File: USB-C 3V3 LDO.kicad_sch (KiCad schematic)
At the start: 6 parts, among them U7 TPS76333

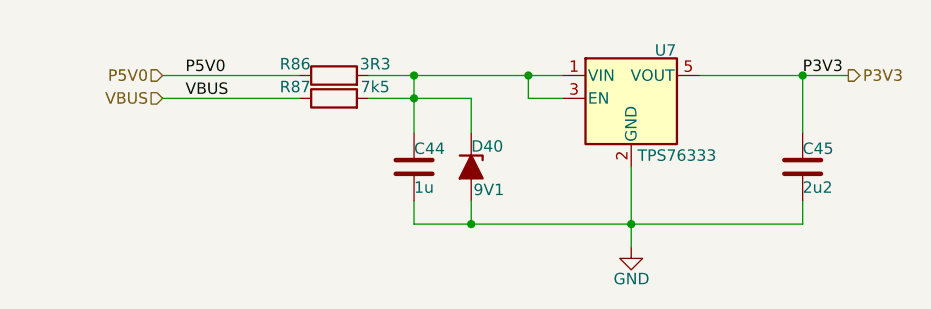
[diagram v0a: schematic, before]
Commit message: Fixed 5V Line
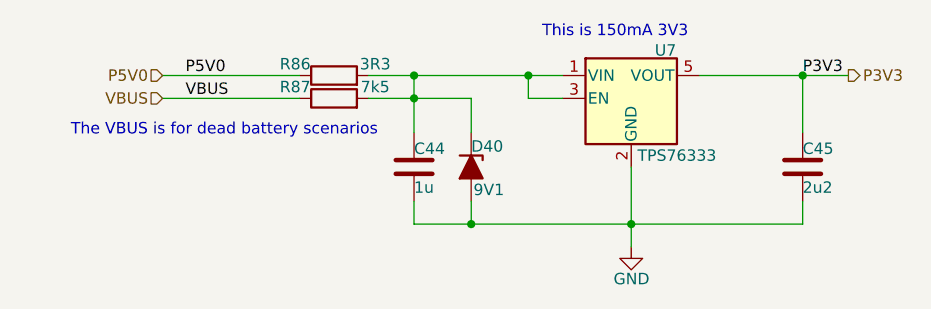
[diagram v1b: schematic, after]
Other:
- note added: "The VBUS is for dead battery scenarios"
- note added: "This is 150mA 3V3"
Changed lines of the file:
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@@
 	(generator_version "9.0")
 	(paper "A4")
+	(text "The VBUS is for dead battery scenarios"
+		(exclude_from_sim no)
+		(at 91.948 100.076 0)
+		(effects
+			(font
+				(size 1.27 1.27)
+			)
+		)
+	)
+	(text "This is 150mA 3V3"
+		(exclude_from_sim no)
+		(at 135.382 89.154 0)
+		(effects
+			(font
+				(size 1.27 1.27)
+			)
+		)
+	)
 	(junction
 		(at 119.38 110.49)
